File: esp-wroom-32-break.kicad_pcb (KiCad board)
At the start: 2 copper layers, 43.2 x 61 mm, 26 parts, among them CON1 Micro_SD_Card, IC1 FT232RQ, P1 CONN_01X17, P2 CONN_01X17, P3 USB_OTG, Q1 MMBT3904, Q2 MMBT3904, SW1 SWITCH_SPST, U1 ESP32-WROOM, U2 NJU7223DL1-33

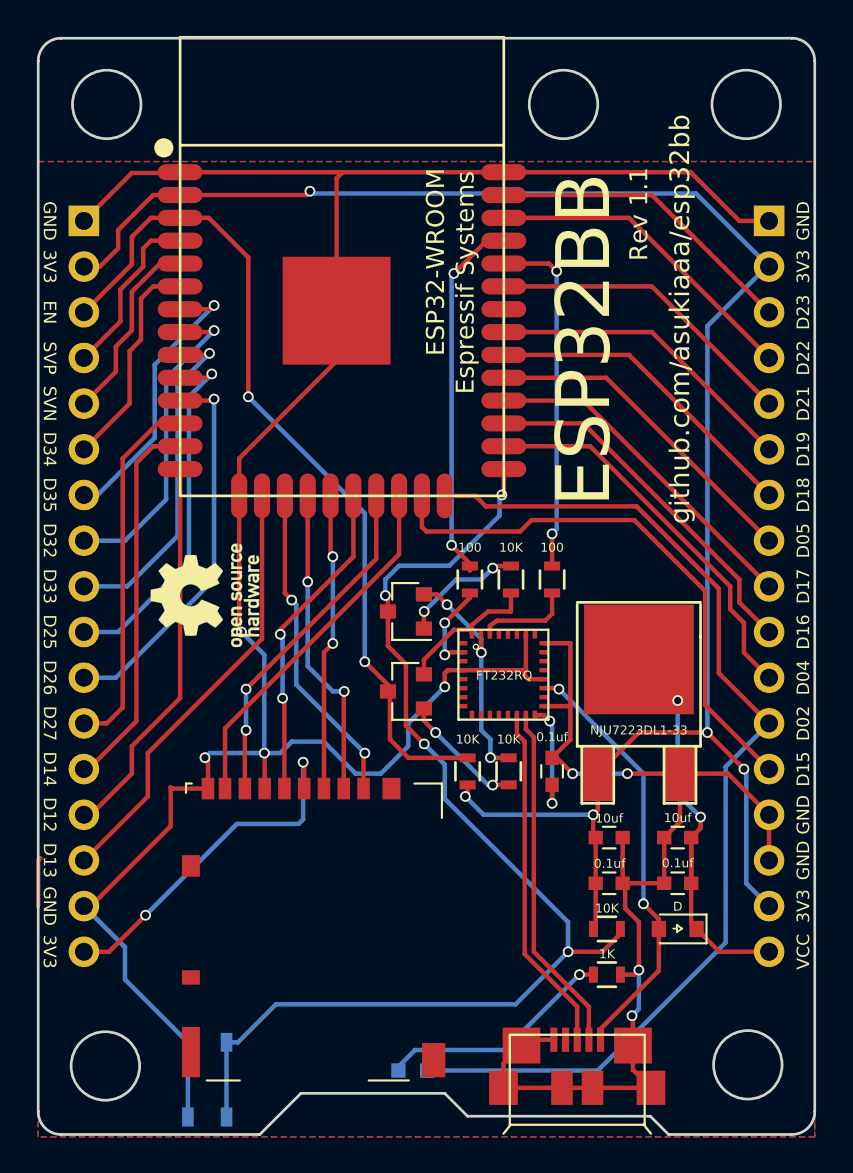
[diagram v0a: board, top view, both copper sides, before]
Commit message: Add registers to pull up SD signals and reset button etc
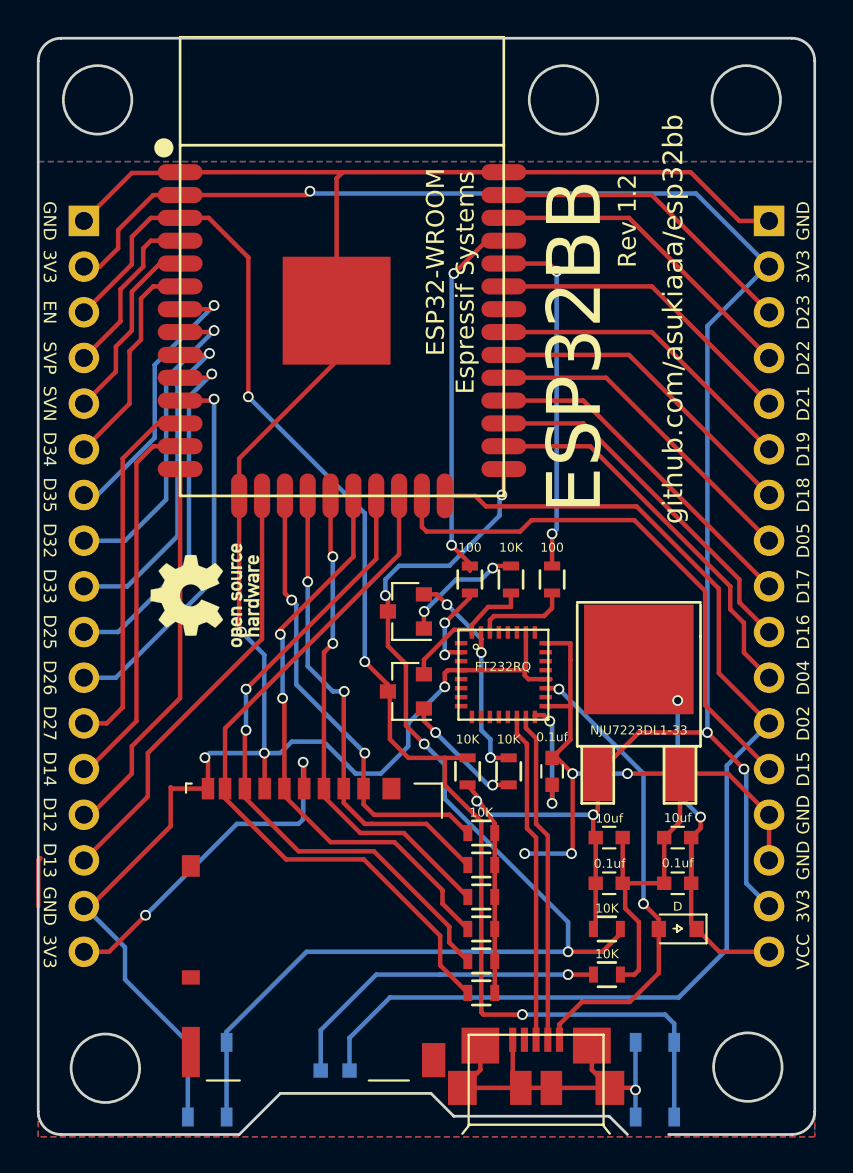
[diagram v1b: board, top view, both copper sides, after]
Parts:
- added R10: 10K, Resistors_SMD:R_0603, F.Cu at (174.5, 110.5)
- added R11: 10K, Resistors_SMD:R_0603, F.Cu at (174.5, 108.7)
- added R12: 10K, Resistors_SMD:R_0603, F.Cu at (174.5, 106.9)
- added R13: 10K, Resistors_SMD:R_0603, F.Cu at (174.5, 105.2)
- added R8: 10K, Resistors_SMD:R_0603, F.Cu at (174.5, 114.0)
- added R9: 10K, Resistors_SMD:R_0603, F.Cu at (174.5, 112.3)
- added SW2: SWITCH_SPST, switch:SKRPACE010, B.Cu at (184.2, 118.9)
- D2: value LED -> D02
- IC1: footprint ftdi232rq:ft232rq -> ftdi232rq:FR232RQ
- R7: value 1K -> 10K
- moved D2 4.32 mm to (166.4, 118.4)
- moved P3 2.29 mm to (177.5, 120.8)
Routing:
- net EN: track 47.9 -> 79.1 mm, vias 2 -> 3
- net SD1: track 20.3 -> 39.8 mm
- net SD0: track 19.3 -> 36.5 mm
- net SD_CLK: track 18.1 -> 32.2 mm
- net +3V3: track 124.7 -> 135.5 mm
- net SD_CMD: track 16.5 -> 27.3 mm
- net GND: track 194.7 -> 204.3 mm, vias 8 -> 9
- net SD3: track 17.5 -> 26.6 mm
- net SD2: track 18.1 -> 25.5 mm
- net IO2: track 58.8 -> 64.4 mm
- net Net-(D2-Pad1): track 13.2 -> 18.7 mm
- net +5V: track 24.0 -> 26.5 mm
- net D-: track 19.5 -> 18.5 mm
- net D+: track 19.4 -> 18.4 mm
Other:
- outline, holes or cut-outs redrawn
- board text added: "D01 PULL UP"
- board text added: "RESET"
- board text added: "Rev 1.2"
- board text removed: "D01 PULLUP"
- board text removed: "Rev 1.1"
